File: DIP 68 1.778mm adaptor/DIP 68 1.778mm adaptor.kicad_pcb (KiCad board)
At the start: 2 copper layers, 34.7 x 81.7 mm, 4 parts, among them J1 Header, J2 Header, U1 DIP-64 1.778mm (0.07") Pitch

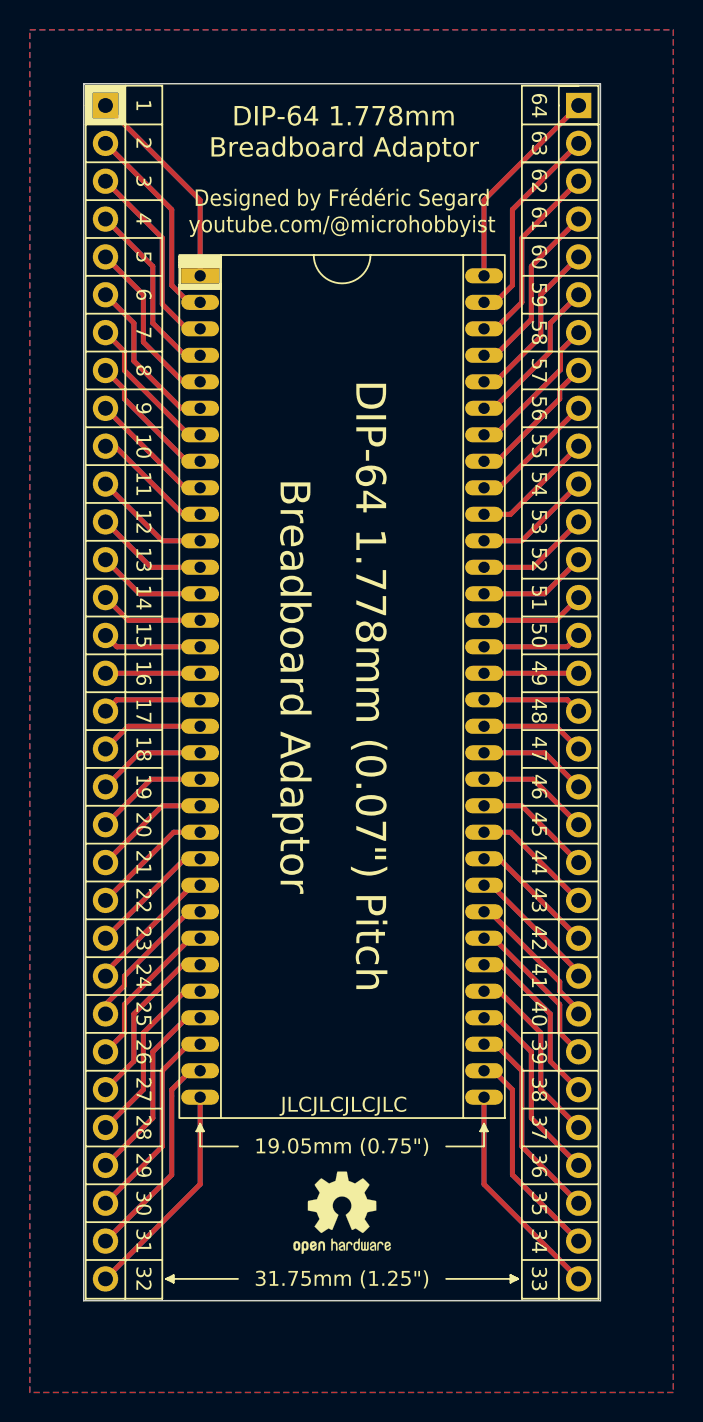
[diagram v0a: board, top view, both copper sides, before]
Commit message: Updated key library and keyboard
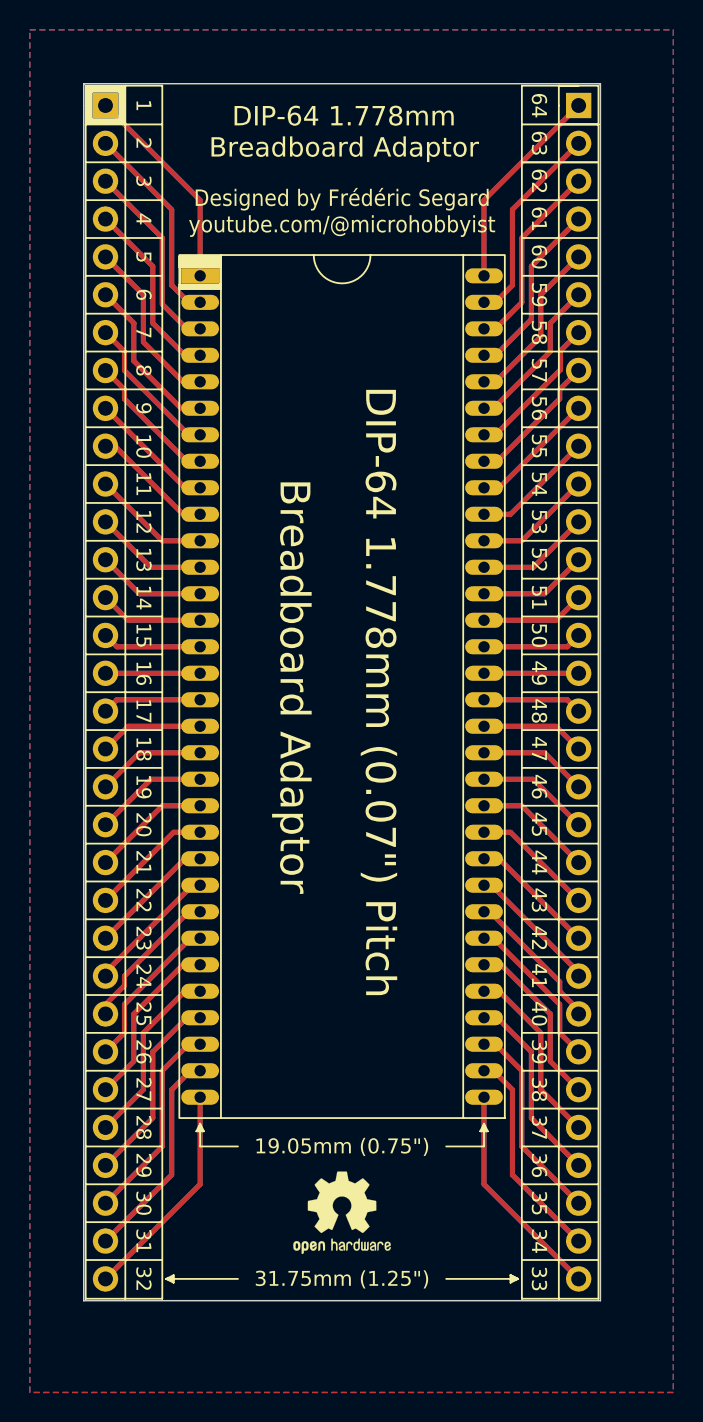
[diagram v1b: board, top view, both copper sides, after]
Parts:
- added G***: LOGO, 0_Z80_Library:JLCPCB Logo 3, B.Cu at (130.3, 84.7)
- U1: value DIP-64 1.778mm (0.07") Pitch -> DIP-64
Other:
- rule pad_to_mask_clearance: 0 -> 0.2
- board text added: "DIP-64 1.778mm (0.07{dblquote}) Pitch"
